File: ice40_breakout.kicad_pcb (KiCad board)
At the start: 2 copper layers, 80 x 100 mm, 100 parts, among them J1 Conn_01x10, J2 Conn_01x08, J3 Conn_01x06, J4 Conn_01x08, J5 USB_B_Micro, SW1 SW_Push, SW2 SW_Push, SW3 SW_Push, SW4 SW_Push, SW5 SW_Push, SW6 SW_Push, U1 ICE40HX4K-TQ144, U2 IS61WV5128EDBLL-10TLI, U3 93LCxxBT-I_OT, U4 FT2232H, U5 IS25LP080D, U6 TLV62568APDRLR, U7 TLV62568APDRLR, U8 TXS0108EPW, U9 TXS0108EPW

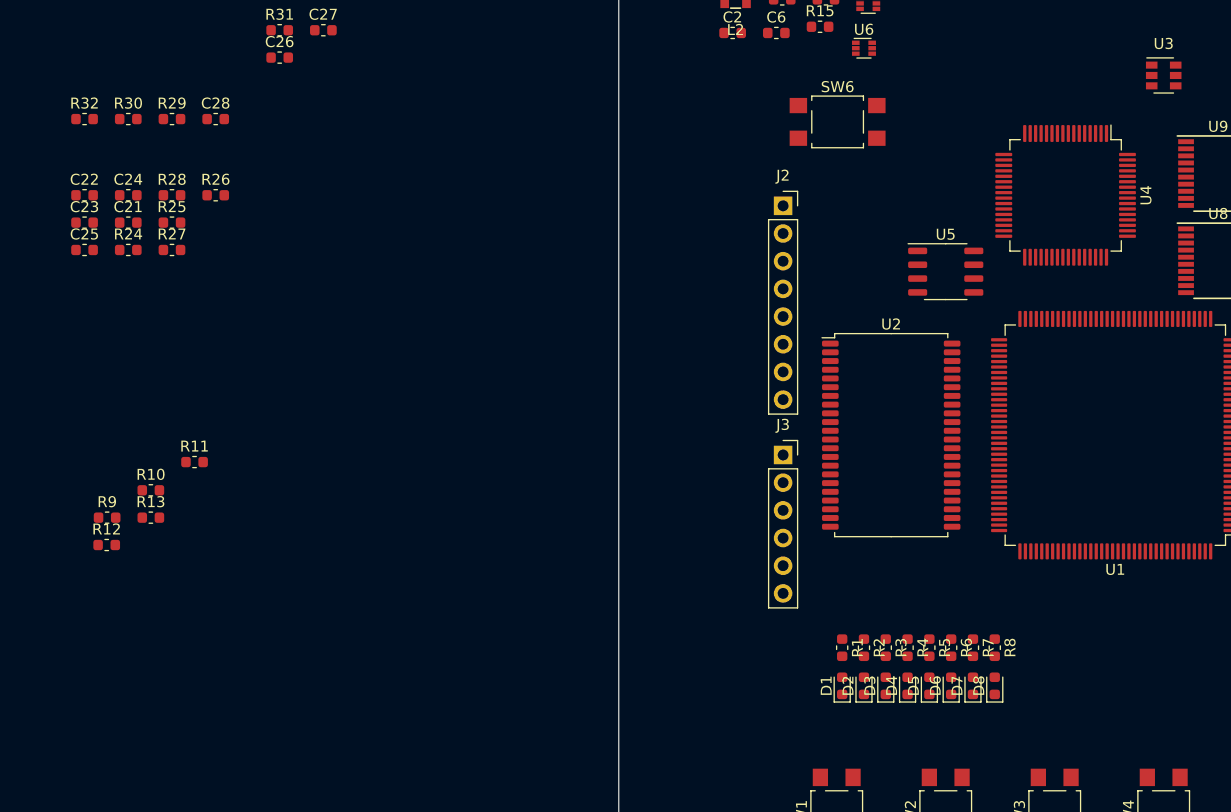
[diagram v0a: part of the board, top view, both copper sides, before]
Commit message: Progress on FTDI - added Oscillator and 1.8 V supply
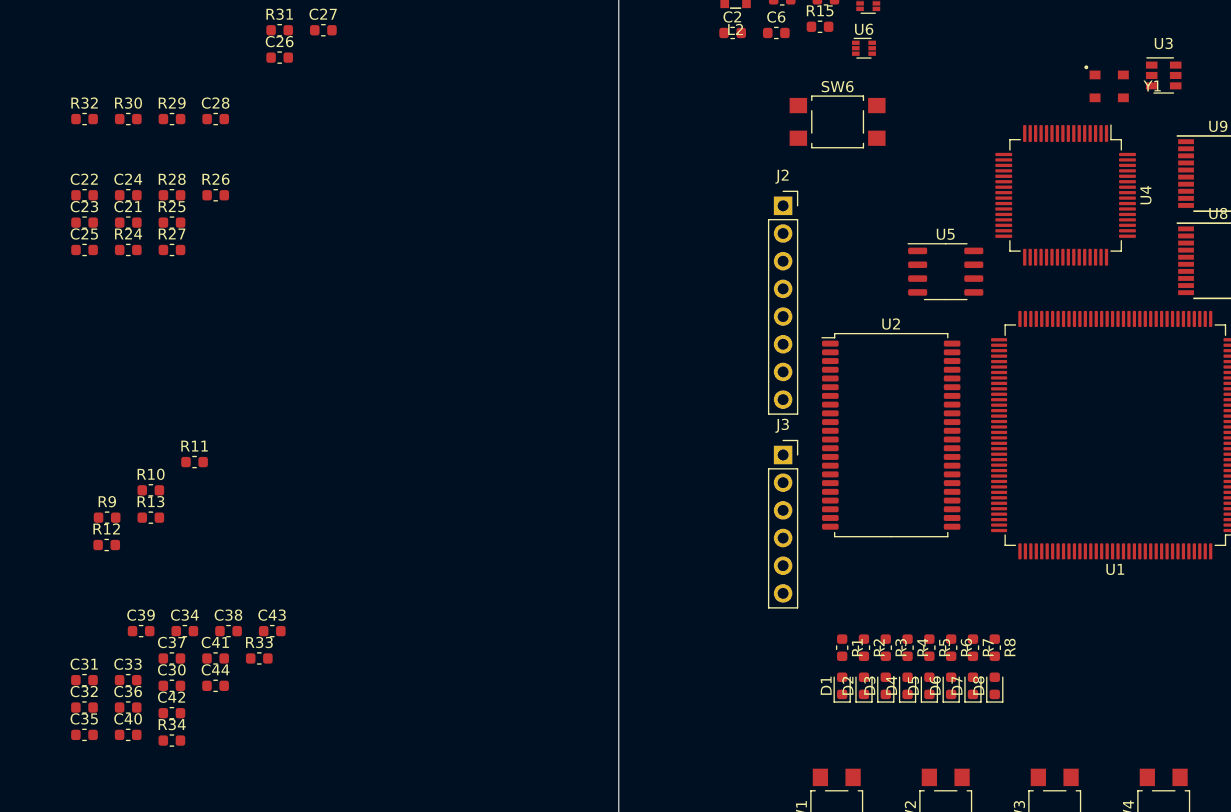
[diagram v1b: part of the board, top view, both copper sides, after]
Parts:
- added C30: 100nF, Capacitor_SMD:C_0603_1608Metric, F.Cu at (59.0, 118.0)
- added C31: 10 uF 6,3 V, Capacitor_SMD:C_0603_1608Metric, F.Cu at (51.0, 117.5)
- added C32: 100nF, Capacitor_SMD:C_0603_1608Metric, F.Cu at (51.0, 120.0)
- added C33: 10 uF 6,3 V, Capacitor_SMD:C_0603_1608Metric, F.Cu at (55.0, 117.5)
- added C34: 10 uF 6,3 V, Capacitor_SMD:C_0603_1608Metric, F.Cu at (60.2, 113.0)
- added C35: 10 uF 6,3 V, Capacitor_SMD:C_0603_1608Metric, F.Cu at (51.0, 122.5)
- added C36: 10 uF 6,3 V, Capacitor_SMD:C_0603_1608Metric, F.Cu at (55.0, 120.0)
- added C37: 10 uF 6,3 V, Capacitor_SMD:C_0603_1608Metric, F.Cu at (59.0, 115.5)
- added C38: 10 uF 6,3 V, Capacitor_SMD:C_0603_1608Metric, F.Cu at (64.2, 113.0)
- added C39: 100nF, Capacitor_SMD:C_0603_1608Metric, F.Cu at (56.2, 113.0)
- added C40: 10 uF 6,3 V, Capacitor_SMD:C_0603_1608Metric, F.Cu at (55.0, 122.5)
- added C41: 10 uF 6,3 V, Capacitor_SMD:C_0603_1608Metric, F.Cu at (63.0, 115.5)
- added C42: 10 uF 6,3 V, Capacitor_SMD:C_0603_1608Metric, F.Cu at (59.0, 120.5)
- added C43: 10 uF 6,3 V, Capacitor_SMD:C_0603_1608Metric, F.Cu at (68.2, 113.0)
- added C44: 10 uF 6,3 V, Capacitor_SMD:C_0603_1608Metric, F.Cu at (63.0, 118.0)
- added R33: 12k, Resistor_SMD:R_0603_1608Metric, F.Cu at (67.0, 115.5)
- added R34: 2,2k, Resistor_SMD:R_0603_1608Metric, F.Cu at (59.0, 123.0)
- added Y1: ECS-3225S33-120-FN-TR, footprints:ECS-3225S_3.2x2.5mm_footprint, F.Cu at (145.0, 63.0)
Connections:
- R23 pad 1: Net-(R23-Pad1) -> Net-(R22-Pad2)
- R23 pad 2: Net-(R22-Pad2) -> Net-(R23-Pad2)
- U1 pad 72: Net-(U1-Pad72) -> +3V3
- U3 pad 1: Net-(R23-Pad1) -> Net-(R22-Pad2)
- U3 pad 3: Net-(R22-Pad2) -> Net-(R23-Pad2)
- U4 pad 12: Net-(U4-Pad12) -> +1V8
- U4 pad 37: Net-(U4-Pad37) -> +1V8
- U4 pad 4: Net-(U4-Pad4) -> +3V3
- U4 pad 49: Net-(U4-Pad49) -> +1V8
- U4 pad 50: Net-(U4-Pad50) -> +3V3
- U4 pad 61: Net-(R22-Pad2) -> Net-(R23-Pad2)
- U4 pad 64: Net-(U4-Pad64) -> +1V8
- U4 pad 9: Net-(U4-Pad9) -> +3V3
- U5 pad 4: Net-(U5-Pad4) -> GND
- U5 pad 8: Net-(U5-Pad8) -> +3V3

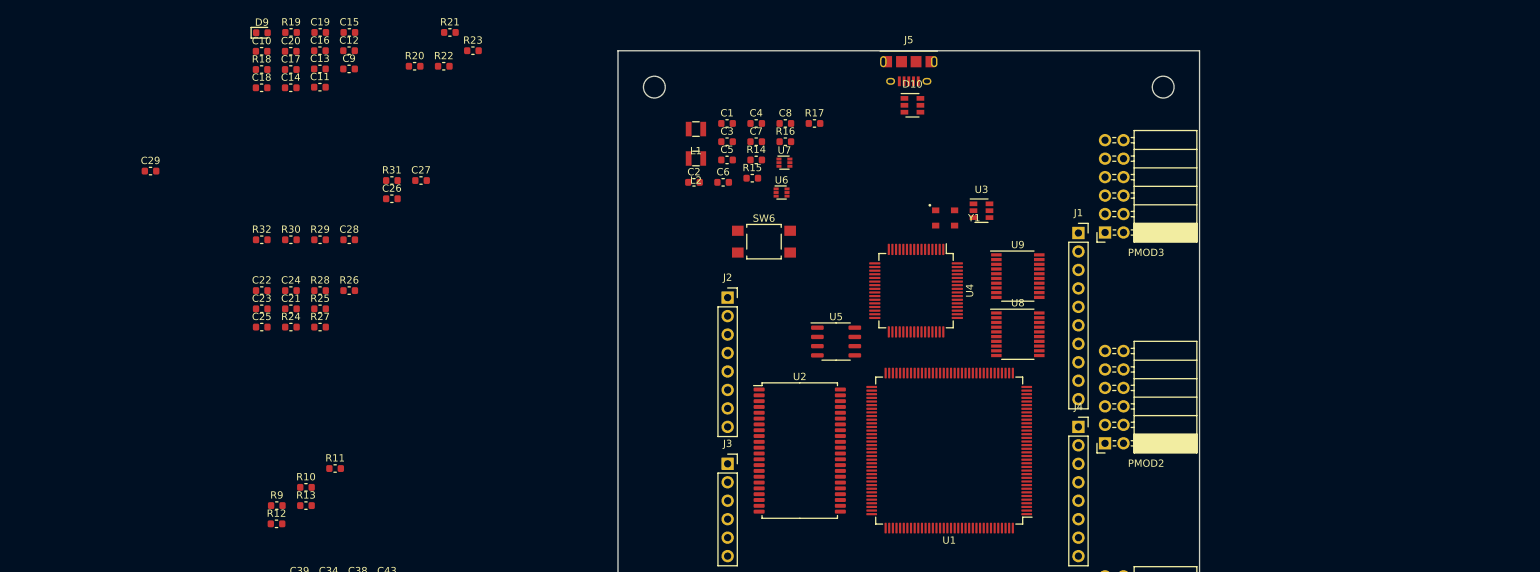
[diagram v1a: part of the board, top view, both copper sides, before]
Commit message: Continued on Programmer, moved the header signals around the package to free some space for a fully featured UART/RS232(TTL)
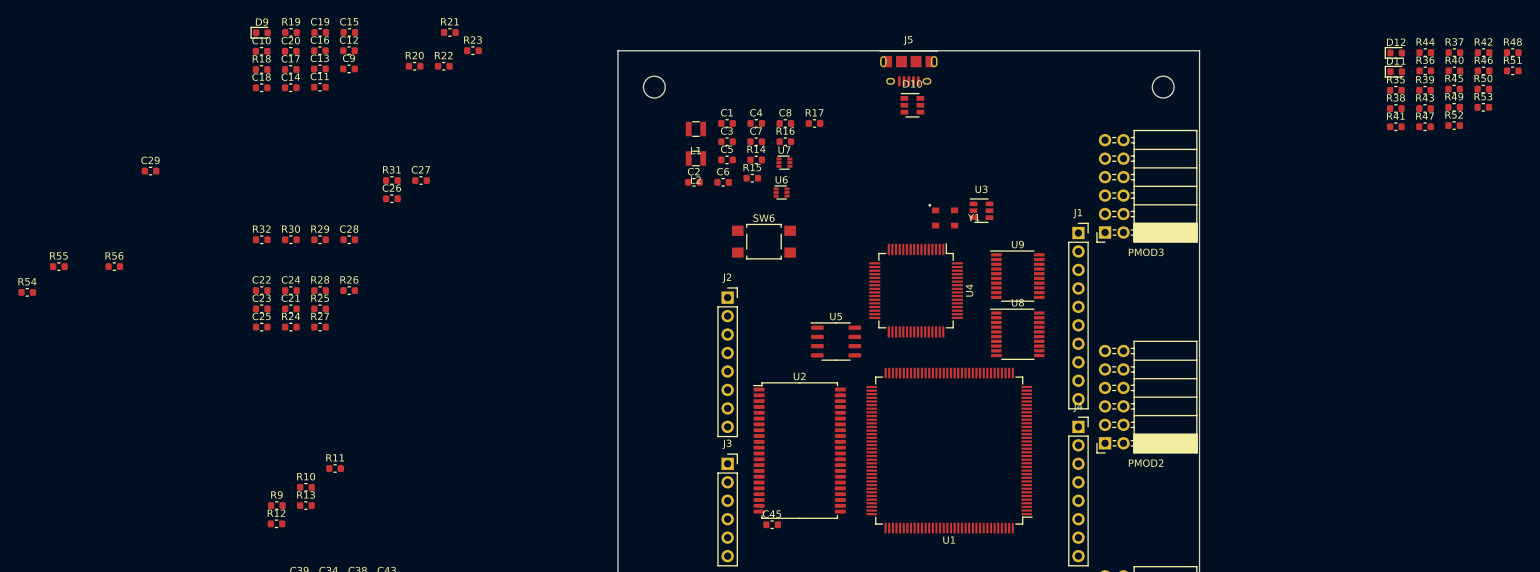
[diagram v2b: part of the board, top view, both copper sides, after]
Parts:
- added C45: 100nF, Capacitor_SMD:C_0603_1608Metric, F.Cu at (121.2, 105.2)
- added D11: RX LED, LED_SMD:LED_0603_1608Metric, F.Cu at (207.0, 42.9)
- added D12: TX LED, LED_SMD:LED_0603_1608Metric, F.Cu at (207.0, 40.3)
- added R35: 0, Resistor_SMD:R_0603_1608Metric, F.Cu at (207.0, 45.4)
- added R36: 0, Resistor_SMD:R_0603_1608Metric, F.Cu at (211.1, 42.8)
- added R37: 0, Resistor_SMD:R_0603_1608Metric, F.Cu at (215.1, 40.3)
- added R38: 10k, Resistor_SMD:R_0603_1608Metric, F.Cu at (207.0, 47.9)
- added R39: 10k, Resistor_SMD:R_0603_1608Metric, F.Cu at (211.0, 45.4)
- added R40: 0, Resistor_SMD:R_0603_1608Metric, F.Cu at (215.1, 42.8)
- added R41: 0, Resistor_SMD:R_0603_1608Metric, F.Cu at (207.0, 50.5)
- added R42: 0, Resistor_SMD:R_0603_1608Metric, F.Cu at (219.1, 40.3)
- added R43: 10k, Resistor_SMD:R_0603_1608Metric, F.Cu at (211.0, 47.9)
- added R44: 10k, Resistor_SMD:R_0603_1608Metric, F.Cu at (211.1, 40.3)
- added R45: 0, Resistor_SMD:R_0603_1608Metric, F.Cu at (215.0, 45.3)
- added R46: 0, Resistor_SMD:R_0603_1608Metric, F.Cu at (219.1, 42.8)
- added R47: 0, Resistor_SMD:R_0603_1608Metric, F.Cu at (211.0, 50.5)
- added R48: 0, Resistor_SMD:R_0603_1608Metric, F.Cu at (223.1, 40.3)
- added R49: 0, Resistor_SMD:R_0603_1608Metric, F.Cu at (215.0, 47.8)
- added R50: 0, Resistor_SMD:R_0603_1608Metric, F.Cu at (219.0, 45.3)
- added R51: 0, Resistor_SMD:R_0603_1608Metric, F.Cu at (223.1, 42.8)
- added R52: 560, Resistor_SMD:R_0603_1608Metric, F.Cu at (215.0, 50.3)
- added R53: 560, Resistor_SMD:R_0603_1608Metric, F.Cu at (219.0, 47.8)
- added R54: 10k, Resistor_SMD:R_0603_1608Metric, F.Cu at (18.7, 73.2)
- added R55: 10k, Resistor_SMD:R_0603_1608Metric, F.Cu at (23.1, 69.7)
- added R56: 0, Resistor_SMD:R_0603_1608Metric, F.Cu at (30.7, 69.7)
- SW1: footprint Button_Switch_SMD:SW_SPST_TL3305A -> footprints:SW_SPST_TL3305A
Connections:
- PMOD1 pad 1: /Header/P7_1 -> P7_1
- PMOD1 pad 2: /Header/P1_1 -> P1_1
- PMOD1 pad 3: /Header/P8_1 -> P8_1
- PMOD1 pad 4: /Header/P2_1 -> P2_1
- PMOD1 pad 5: /Header/P9_1 -> P9_1
- PMOD1 pad 6: /Header/P3_1 -> P3_1
- PMOD1 pad 7: /Header/P10_1 -> P10_1
- PMOD1 pad 8: /Header/P4_1 -> P4_1
- SW6 pad 1: Net-(SW6-Pad1) -> GND
- SW6 pad 2: Net-(SW6-Pad2) -> CRESET_B
- U1 pad 1: /Header/P1_1 -> /Header/P1_2
- U1 pad 10: /Header/P10_1 -> /Header/P10_2
- U1 pad 11: /Header/P1_2 -> /Header/P1_3
- U1 pad 110: /User Interface/LED0 -> ~SRAM_CE~
- U1 pad 112: /User Interface/LED1 -> /User Interface/LED0
- U1 pad 113: /User Interface/LED2 -> /User Interface/LED1
- U1 pad 114: /User Interface/LED3 -> /User Interface/LED2
- U1 pad 115: /User Interface/LED4 -> /User Interface/LED3
- U1 pad 116: /User Interface/LED5 -> /User Interface/LED4
- U1 pad 117: /User Interface/LED6 -> /User Interface/LED5
- U1 pad 118: /User Interface/LED7 -> /User Interface/LED6
- U1 pad 119: Net-(U1-Pad119) -> /User Interface/LED7
- U1 pad 12: /Header/P2_2 -> /Header/P2_3
- U1 pad 120: Net-(U1-Pad120) -> /User Interface/SW0
- U1 pad 121: Net-(U1-Pad121) -> /User Interface/SW1
- U1 pad 122: Net-(U1-Pad122) -> /User Interface/SW2
- U1 pad 124: Net-(U1-Pad124) -> /User Interface/SW3
- U1 pad 125: Net-(U1-Pad125) -> /User Interface/SW4
- U1 pad 128: Net-(U1-Pad128) -> /User Interface/SW5
- U1 pad 130: /User Interface/SW0 -> Net-(U1-Pad130)
- U1 pad 134: /User Interface/SW1 -> Net-(U1-Pad134)
- U1 pad 135: /User Interface/SW2 -> Net-(U1-Pad135)
- U1 pad 136: /User Interface/SW3 -> P1_1
- U1 pad 137: /User Interface/SW4 -> P2_1
- U1 pad 138: /User Interface/SW5 -> P3_1
- U1 pad 139: Net-(U1-Pad139) -> P4_1
- U1 pad 141: Net-(U1-Pad141) -> P7_1
- U1 pad 142: Net-(U1-Pad142) -> P8_1
- U1 pad 143: Net-(U1-Pad143) -> P9_1
- U1 pad 144: ~SRAM_CE~ -> P10_1
- U1 pad 15: /Header/P3_2 -> /Header/P3_3
- U1 pad 16: /Header/P4_2 -> /Header/P4_3
- U1 pad 17: /Header/P7_2 -> /Header/P7_3
- U1 pad 18: /Header/P8_2 -> /Header/P8_3
- U1 pad 19: /Header/P9_2 -> /Header/P9_3
- U1 pad 2: /Header/P2_1 -> /Header/P2_2
- U1 pad 20: Net-(U1-Pad20) -> /Header/P10_3
- U1 pad 21: Net-(U1-Pad21) -> ICE_CLK_12M
- U1 pad 22: /Header/P10_2 -> Net-(U1-Pad22)
- U1 pad 23: /Header/P1_3 -> Net-(U1-Pad23)
- U1 pad 24: /Header/P2_3 -> /Header/FPGA_INO_SCL
- U1 pad 25: /Header/P3_3 -> /Header/FPGA_INO_SDA
- U1 pad 26: /Header/P4_3 -> /Header/FPGA_INO_SCK
- U1 pad 28: /Header/P7_3 -> /Header/FPGA_INO_MISO
- U1 pad 29: /Header/P8_3 -> /Header/FPGA_INO_MOSI
- U1 pad 3: /Header/P3_1 -> /Header/P3_2
- U1 pad 31: /Header/P9_3 -> /Header/FPGA_INO_SS
- U1 pad 32: /Header/P10_3 -> /Header/FPGA_INO_D9
- U1 pad 33: Net-(U1-Pad33) -> /Header/FPGA_INO_D8
- U1 pad 4: /Header/P4_1 -> /Header/P4_2
- U1 pad 48: /Header/FPGA_INO_SCL -> TXD
- U1 pad 49: /Header/FPGA_INO_SDA -> RXD
- U1 pad 52: /Header/FPGA_INO_SCK -> Net-(U1-Pad52)
- U1 pad 55: /Header/FPGA_INO_MISO -> ~RTS~
- U1 pad 56: /Header/FPGA_INO_MOSI -> ~CTS~
- U1 pad 60: /Header/FPGA_INO_SS -> ~DTR~
- U1 pad 61: /Header/FPGA_INO_D9 -> ~DSR~
- U1 pad 62: /Header/FPGA_INO_D8 -> ~DCD~
- U1 pad 65: Net-(U1-Pad65) -> CDONE
- U1 pad 66: Net-(U1-Pad66) -> CRESET_B
- U1 pad 7: /Header/P7_1 -> /Header/P7_2
- U1 pad 8: /Header/P8_1 -> /Header/P8_2
- U1 pad 9: /Header/P9_1 -> /Header/P9_2
- U2 pad 11: Net-(U2-Pad11) -> +3V3
- U2 pad 12: Net-(U2-Pad12) -> GND
- U2 pad 33: Net-(U2-Pad11) -> +3V3
- U2 pad 34: Net-(U2-Pad12) -> GND
- U4 pad 13: Net-(U4-Pad13) -> GND

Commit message: Added switches, added 5 V rail and 17 V input(with filtering). Power is mostly done.
Also added a first version of buffers to ftdi chip. I'll change the evtl.

Started to route power section.
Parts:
- added C34: 10 uF 25 V, Capacitor_SMD:C_0805_2012Metric, B.Cu at (115.7, 52.7)
- added C35: 100nF, Capacitor_SMD:C_0603_1608Metric, B.Cu at (115.7, 54.5)
- added C36: 100nF, Capacitor_SMD:C_0603_1608Metric, F.Cu at (111.0, 50.0)
- added C37: 10 uF 25 V, Capacitor_SMD:C_0805_2012Metric, F.Cu at (108.5, 55.5)
- added C38: 10 uF 25 V, Capacitor_SMD:C_0805_2012Metric, F.Cu at (108.5, 53.5)
- added C41: 100nF, Capacitor_SMD:C_0603_1608Metric, F.Cu at (108.8, 57.2)
- added C42: 100nF, Capacitor_SMD:C_0603_1608Metric, F.Cu at (16.8, 102.7)
- added C43: 100nF, Capacitor_SMD:C_0603_1608Metric, F.Cu at (108.5, 62.8)
- added C44: 22 uF 6,3 V, Capacitor_SMD:C_0603_1608Metric, F.Cu at (117.2, 57.8)
- added C46: 1 uF 16 V, Capacitor_SMD:C_0603_1608Metric, F.Cu at (53.0, 138.0)
- added C47: 1 uF 16 V, Capacitor_SMD:C_0603_1608Metric, F.Cu at (49.0, 141.6)
- added C48: 22 uF 6,3 V, Capacitor_SMD:C_0603_1608Metric, F.Cu at (118.7, 57.8)
- added C49: 10pF, Capacitor_SMD:C_0603_1608Metric, F.Cu at (103.8, 57.7)
- added C50: 10 uF 6,3 V, Capacitor_SMD:C_0603_1608Metric, F.Cu at (-1.44, 103.2)
- added C51: 100nF, Capacitor_SMD:C_0603_1608Metric, F.Cu at (3.76, 98.4)
- added C52: 10 uF 6,3 V, Capacitor_SMD:C_0603_1608Metric, F.Cu at (-5.69, 107.7)
- added C53: 100nF, Capacitor_SMD:C_0603_1608Metric, F.Cu at (7.77, 93.7)
- added C54: 10 uF 6,3 V, Capacitor_SMD:C_0603_1608Metric, F.Cu at (149.5, 50.8)
- added C55: 10 uF 6,3 V, Capacitor_SMD:C_0603_1608Metric, F.Cu at (28.9, 116.3)
- added C56: 100nF, Capacitor_SMD:C_0603_1608Metric, F.Cu at (25.6, 108.4)
- added C57: 100nF, Capacitor_SMD:C_0603_1608Metric, F.Cu at (16.8, 116.8)
- added C58: 100nF, Capacitor_SMD:C_0603_1608Metric, F.Cu at (20.8, 114.3)
- added C59: 100nF, Capacitor_SMD:C_0603_1608Metric, F.Cu at (25.2, 111.3)
- added C60: 100nF, Capacitor_SMD:C_0603_1608Metric, F.Cu at (16.8, 119.3)
- added C61: 100nF, Capacitor_SMD:C_0603_1608Metric, F.Cu at (29.7, 108.4)
- added C62: 100nF, Capacitor_SMD:C_0603_1608Metric, F.Cu at (37.7, 108.4)
- added C63: 100nF, Capacitor_SMD:C_0603_1608Metric, F.Cu at (32.9, 113.4)
- added C64: 100nF, Capacitor_SMD:C_0603_1608Metric, F.Cu at (24.9, 118.9)
- added C65: 10 uF 6,3 V, Capacitor_SMD:C_0603_1608Metric, F.Cu at (33.3, 110.9)
- added C66: 100nF, Capacitor_SMD:C_0603_1608Metric, F.Cu at (28.9, 113.8)
- added C67: 100nF, Capacitor_SMD:C_0603_1608Metric, F.Cu at (24.9, 116.3)
- added C68: 100nF, Capacitor_SMD:C_0603_1608Metric, F.Cu at (33.7, 108.4)
- added C69: 100nF, Capacitor_SMD:C_0603_1608Metric, F.Cu at (20.8, 119.3)
- added C70: 100nF, Capacitor_SMD:C_0603_1608Metric, F.Cu at (29.3, 110.9)
- added C71: 100nF, Capacitor_SMD:C_0603_1608Metric, F.Cu at (16.8, 114.3)
- added C72: 100nF, Capacitor_SMD:C_0603_1608Metric, F.Cu at (20.8, 116.8)
- added C73: 100nF, Capacitor_SMD:C_0603_1608Metric, F.Cu at (-19.5, 115.9)
- added C74: 100nF, Capacitor_SMD:C_0603_1608Metric, F.Cu at (37.1, 91.2)
- added D13: CDBU5020, Diode_SMD:D_0603_1608Metric, F.Cu at (-5.45, 102.4)
- added FB1: 330 Ohm, Resistor_SMD:R_0805_2012Metric, B.Cu at (118.4, 51.5)
- added FB2: 330 Ohm, Resistor_SMD:R_0805_2012Metric, B.Cu at (112.9, 51.5)
- added FB3: 330 Ohm, Resistor_SMD:R_0805_2012Metric, F.Cu at (153.0, 47.5)
- added FB4: 330 Ohm, Resistor_SMD:R_0805_2012Metric, F.Cu at (17.0, 111.5)
- added FB5: 330 Ohm, Resistor_SMD:R_0805_2012Metric, F.Cu at (17.0, 108.6)
- added FB6: 330 Ohm, Resistor_SMD:R_0805_2012Metric, F.Cu at (146.0, 47.5)
- added J6: 7-17 V IN, TerminalBlock:TerminalBlock_bornier-2_P5.08mm, F.Cu at (113.2, 44.2)
- added JP1: Jumper_NO_Small, Connector_PinHeader_2.54mm:PinHeader_1x02_P2.54mm_Vertical, F.Cu at (-14.2, 101.3)
- added L3: L_DLW5BTM, footprints:DLW5BTM_5.00x5.00mm_footprint, F.Cu at (115.4, 52.0)
- added L4: 4,7 uH, Inductor_SMD:L_Taiyo-Yuden_NR-50xx, F.Cu at (113.5, 59.0)
- added Q1: DMP3099L-7, Package_TO_SOT_SMD:SOT-23, F.Cu at (108.5, 50.0)
- added Q1: 2N7002, Package_TO_SOT_SMD:SOT-23, F.Cu at (53.2, 134.5)
- added R35: 54k9 1%, Resistor_SMD:R_0603_1608Metric, F.Cu at (103.8, 59.2)
- added R35: 10k, Resistor_SMD:R_0603_1608Metric, F.Cu at (49.0, 144.1)
- added R36: 4k7, Resistor_SMD:R_0603_1608Metric, F.Cu at (53.1, 140.5)
- added R37: 10k, Resistor_SMD:R_0603_1608Metric, F.Cu at (53.1, 143.0)
- added R40: 10k 1%, Resistor_SMD:R_0603_1608Metric, F.Cu at (103.8, 60.7)
- added R41: 100, Resistor_SMD:R_0603_1608Metric, F.Cu at (6.40, 91.2)
- added R42: 100, Resistor_SMD:R_0603_1608Metric, F.Cu at (6.58, 103.8)
- added R45: 10k, Resistor_SMD:R_0603_1608Metric, F.Cu at (156.0, 44.5)
- added R46: 33k, Resistor_SMD:R_0603_1608Metric, F.Cu at (6.58, 101.3)
- added R47: 10k, Resistor_SMD:R_0603_1608Metric, F.Cu at (2.33, 105.8)
- added R48: 10k, Resistor_SMD:R_0603_1608Metric, F.Cu at (-1.68, 108.3)
- added R49: 22k, Resistor_SMD:R_0603_1608Metric, F.Cu at (7.77, 98.8)
- added R50: 4,7k, Resistor_SMD:R_0603_1608Metric, F.Cu at (20.8, 100.2)
- added R51: 4,7k, Resistor_SMD:R_0603_1608Metric, F.Cu at (16.8, 100.2)
- added R56: 470, Resistor_SMD:R_0603_1608Metric, F.Cu at (20.8, 102.7)
- added R57: 470, Resistor_SMD:R_0603_1608Metric, F.Cu at (24.9, 100.2)
- added RV1: CG0603MLA-18KE, Resistor_SMD:R_0603_1608Metric, B.Cu at (115.7, 49.0)
- added RV2: CG0603MLA-18KE, Resistor_SMD:R_0603_1608Metric, B.Cu at (115.7, 50.5)
- added SW7: JS202011SCQN, footprints:SW_SLIDE_DPDT_Slide_CK_JS202011SCQN_W3mm_P2.5mm_footprint, F.Cu at (93.5, 78.5)
- added SW8: JS202011SCQN, footprints:SW_SLIDE_DPDT_Slide_CK_JS202011SCQN_W3mm_P2.5mm_footprint, F.Cu at (144.4, 116.5)
- added SW9: JS202011SCQN, footprints:SW_SLIDE_DPDT_Slide_CK_JS202011SCQN_W3mm_P2.5mm_footprint, F.Cu at (154.6, 116.5)
- added U10: MAX40200AUK, Package_TO_SOT_SMD:SOT-23-5, F.Cu at (63.0, 134.5)
- added U11: TXS0108EPW, Package_SO:TSSOP-20_4.4x6.5mm_P0.65mm, F.Cu at (134.0, 76.5)
- added U12: TPS562201, Package_TO_SOT_SMD:SOT-23-6, F.Cu at (108.5, 60.0)
- added U12: MAX40200AUK, Package_TO_SOT_SMD:SOT-23-5, F.Cu at (35.5, 142.7)
- added U13: TXS0108EPW, Package_SO:TSSOP-20_4.4x6.5mm_P0.65mm, F.Cu at (144.5, 76.5)
- added U14: MIC5365-3.3YC5, Package_TO_SOT_SMD:SOT-353_SC-70-5, F.Cu at (156.0, 47.5)
- added U15: MAX40200AUK, Package_TO_SOT_SMD:SOT-23-5, F.Cu at (121.5, 58.0)
- added U15: MAX40200AUK, Package_TO_SOT_SMD:SOT-23-5, F.Cu at (40.4, 142.7)
- added Y2: ECS-3225S33-500-FN-TR, footprints:ECS-3225S_3.2x2.5mm_footprint, F.Cu at (-23.9, 117.1)
- moved C2 93.7 mm to (17.9, 43.1)
- moved R14 93.7 mm to (26.5, 40.0)
- moved R15 93.7 mm to (26.0, 42.5)
- moved U6 93.7 mm to (30.0, 44.5)
- moved U4 78.5 mm to (219.5, 73.5)
- moved C1 38.8 mm to (134.5, 16.5)
- moved C3 36.8 mm to (134.0, 21.0)
- moved L1 35.1 mm to (134.5, 25.0), turned to 90 degrees
- moved C4 34.0 mm to (134.0, 19.5)
- moved C6 26.3 mm to (120.0, 32.4), turned to 90 degrees
- moved C5 25.0 mm to (115.0, 30.0)
- moved U7 24.4 mm to (115.0, 32.2), turned to 270 degrees
- moved L2 20.9 mm to (112.0, 34.0), turned to 270 degrees
- moved R16 20.7 mm to (118.5, 32.4), turned to 90 degrees
- moved R17 20.3 mm to (117.0, 32.4), turned to 270 degrees
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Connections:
- net /User Interface/SW0 renamed Net-(U1-Pad120)
- net Net-(D10-Pad5) renamed /USB Programmer/VBUS_IN
- C1 pad 1: Net-(C1-Pad1) -> +5V
- C30 pad 1: +3V3 -> /USB Programmer/V_USB_PLL
- C31 pad 1: +3V3 -> /USB Programmer/V_USB_PLL
- C32 pad 1: +3V3 -> /USB Programmer/V_USB_PHY
- C33 pad 1: +3V3 -> /USB Programmer/V_USB_PHY
- C34 pad 1: +3V3 -> +3V3_FTDI
- C35 pad 1: +3V3 -> +3V3_FTDI
- C36 pad 1: +3V3 -> +3V3_FTDI
- C37 pad 1: +3V3 -> +3V3_FTDI
- C38 pad 1: +3V3 -> +3V3_FTDI
- C43 pad 1: +3V3 -> +3V3_FTDI
- C44 pad 1: +3V3 -> +3V3_FTDI
- C5 pad 1: Net-(C5-Pad1) -> +5V
- D10 pad 1: /USB Programmer/D_P -> /USB Programmer/D_N
- D10 pad 2: GND -> /USB Programmer/GNDBUS
- D10 pad 6: /USB Programmer/D_N -> /USB Programmer/D_P
- J5 pad 2: /USB Programmer/D_N -> /USB Programmer/D_P
- J5 pad 3: /USB Programmer/D_P -> /USB Programmer/D_N
- J5 pad 5: GND -> /USB Programmer/GNDBUS
- R20 pad 1: +3V3 -> +3V3_FTDI
- R21 pad 1: +3V3 -> +3V3_FTDI
- R22 pad 1: +3V3 -> +3V3_FTDI
- R33 pad 1: +3V3 -> GND
- R34 pad 1: GND -> +3V3_FTDI
- R52 pad 1: +3V3 -> +3V3_FTDI
- R53 pad 1: +3V3 -> +3V3_FTDI
- U1 pad 121: /User Interface/SW1 -> Net-(U1-Pad121)
- U1 pad 122: /User Interface/SW2 -> /User Interface/SW1
- U1 pad 124: /User Interface/SW3 -> /User Interface/SW2
- U1 pad 125: /User Interface/SW4 -> /User Interface/SW3
- U1 pad 126: Net-(U1-Pad126) -> /power/VCCPLL_1
- U1 pad 127: Net-(U1-Pad127) -> /power/GNDPLL_1
- U1 pad 128: /User Interface/SW5 -> /User Interface/SW4
- U1 pad 129: Net-(U1-Pad129) -> /User Interface/SW5
- U1 pad 130: Net-(U1-Pad130) -> /User Interface/SW6
- U1 pad 134: Net-(U1-Pad134) -> /User Interface/SW7
- U1 pad 52: Net-(U1-Pad52) -> /Header/IC_CLK_50M
- U1 pad 53: Net-(U1-Pad53) -> /power/GNDPLL_0
- U1 pad 54: Net-(U1-Pad54) -> /power/VCCPLL_0
- U3 pad 6: +3V3 -> +3V3_FTDI
- U4 pad 16: Net-(R35-Pad1) -> Net-(U11-Pad1)
- U4 pad 17: Net-(R36-Pad1) -> Net-(U11-Pad3)
- U4 pad 18: Net-(R37-Pad1) -> Net-(U11-Pad4)
- U4 pad 2: Net-(R56-Pad2) -> /USB Programmer/12_MHZ
- U4 pad 20: +3V3 -> +3V3_FTDI
- U4 pad 21: Net-(R40-Pad1) -> Net-(U11-Pad5)
- U4 pad 23: Net-(R41-Pad1) -> Net-(U11-Pad6)
- U4 pad 24: Net-(R42-Pad1) -> Net-(U11-Pad7)
- U4 pad 31: +3V3 -> +3V3_FTDI
- U4 pad 38: Net-(R45-Pad1) -> Net-(U11-Pad8)
- U4 pad 39: Net-(R46-Pad1) -> Net-(U11-Pad9)
- U4 pad 4: +3V3 -> /USB Programmer/V_USB_PHY
- U4 pad 40: Net-(R47-Pad1) -> Net-(U13-Pad1)
- U4 pad 41: Net-(R48-Pad1) -> Net-(U13-Pad3)
- U4 pad 42: +3V3 -> +3V3_FTDI
- U4 pad 43: Net-(R49-Pad1) -> Net-(U13-Pad4)
- U4 pad 44: Net-(R50-Pad1) -> Net-(U13-Pad5)
- U4 pad 45: Net-(R51-Pad1) -> Net-(U13-Pad6)
- U4 pad 50: +3V3 -> +3V3_FTDI
- U4 pad 56: +3V3 -> +3V3_FTDI
- U4 pad 9: +3V3 -> /USB Programmer/V_USB_PLL
- U6 pad 3: Net-(C1-Pad1) -> +5V
- U6 pad 5: Net-(C1-Pad1) -> /power/EN_LOW_VOLTAGE
- U7 pad 3: Net-(C5-Pad1) -> +5V
- U7 pad 5: Net-(C5-Pad1) -> /power/EN_LOW_VOLTAGE
- Y1 pad 1: Net-(Y1-Pad1) -> +3V3_FTDI
- Y1 pad 4: Net-(R56-Pad2) -> /USB Programmer/12_MHZ
- Y1 pad 6: +3V3 -> +3V3_FTDI
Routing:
- net /USB Programmer/VBUS_IN: track 0.00 -> 10.4 mm
- net /USB Programmer/GNDBUS: track 0.00 -> 10.4 mm
- net +3V3: track 0.00 -> 7.94 mm, vias 0 -> 2
- net /power/FB_3V3: track 0.00 -> 4.53 mm
- net VBUS: track 0.00 -> 4.17 mm
- net PG: track 0.00 -> 1.10 mm, vias 0 -> 1
- net GND: track 0.00 -> 0.85 mm, vias 0 -> 11
- net /power/EN_LOW_VOLTAGE: track 0.00 -> 0.75 mm, vias 0 -> 1
- added copper zone on F.Cu, net +3V3
- added copper zone on F.Cu, net GND
- added copper zone on In1.Cu, net GND
- added copper zone on F.Cu, net Net-(L2-Pad1)
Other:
- copper layers 2 -> 4
- net class Default: clearance 0.2 -> 0.15; trace_width 0.25 -> 0.15; via_dia 0.8 -> 0.6; via_drill 0.4 -> 0.3
- net class USB_PWR added: clearance 0.2, trace_width 0.4, via_dia 0.6, via_drill 0.3
- rule trace_clearance: 0.2 -> 0.15
- rule trace_min: 0.2 -> 0.15
